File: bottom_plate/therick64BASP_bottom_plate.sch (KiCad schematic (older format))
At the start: 80 parts, among them U1 HOLE, U10 HOLE, U11 HOLE, U12 HOLE, U13 HOLE, U14 HOLE, U15 HOLE, U16 HOLE, U17 HOLE, U18 HOLE, U19 HOLE, U2 HOLE, U20 HOLE, U21 HOLE, U22 HOLE, U23 HOLE, U24 HOLE, U25 HOLE, U26 HOLE, U27 HOLE, U28 HOLE, U29 HOLE, U3 HOLE, U30 HOLE, U31 HOLE, U32 HOLE, U33 HOLE, U34 HOLE, U35 HOLE, U36 HOLE, U37 HOLE, U38 HOLE, U39 HOLE, U4 HOLE, U40 HOLE, U41 HOLE, U42 HOLE, U43 HOLE, U44 HOLE, U45 HOLE, U46 HOLE, U47 HOLE, U48 HOLE, U49 HOLE, U5 HOLE, U50 HOLE, U51 HOLE, U52 HOLE, U53 HOLE, U54 HOLE, U55 HOLE, U56 HOLE, U57 HOLE, U58 HOLE, U59 HOLE, U6 HOLE, U60 HOLE, U61 HOLE, U62 HOLE, U63 HOLE, U64 HOLE, U65 HOLE, U66 HOLE, U67 HOLE, U68 HOLE, U69 HOLE, U7 HOLE, U70 HOLE, U8 HOLE, U9 HOLE

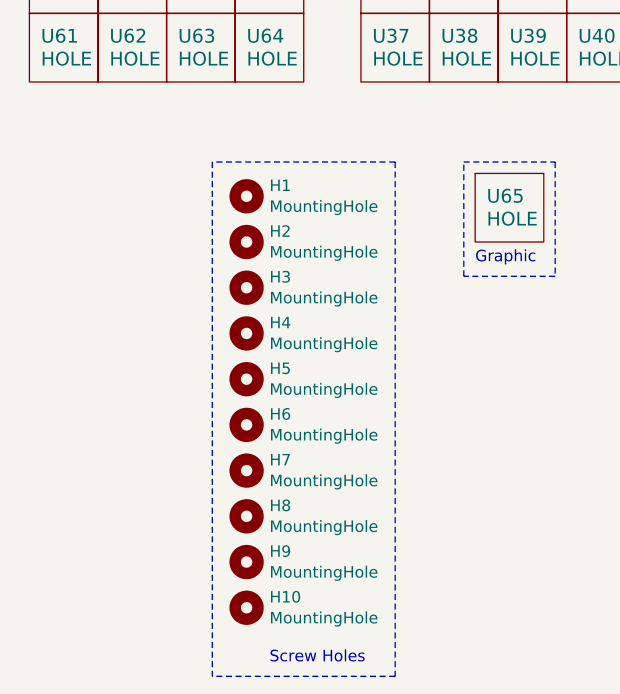
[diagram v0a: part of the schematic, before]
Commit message: Remapped ISP Flash, added mounting holes
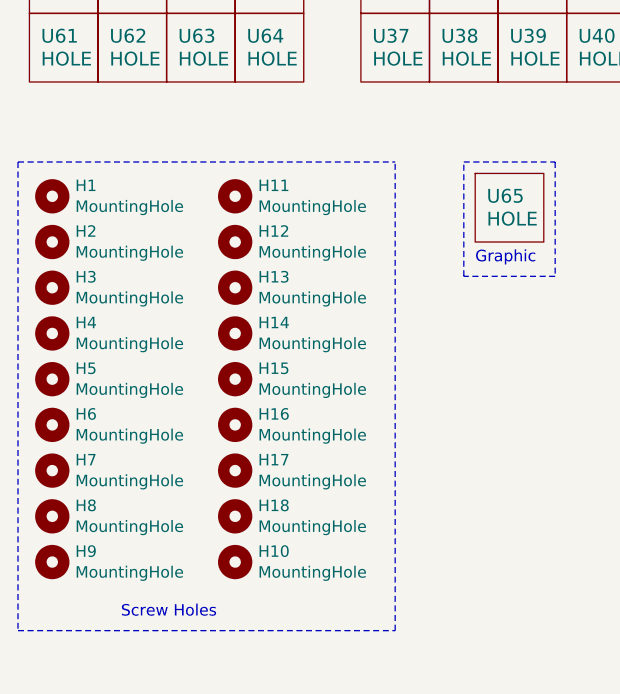
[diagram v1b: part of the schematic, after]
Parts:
- added H11, H12, H13, H14, H15, H16, H17, H18: MountingHole, random-keyboard-parts:Generic-Mounthole, symbol Mechanical:MountingHole
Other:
- moved on the sheet: H1, H10, H2, H3, H4, H5, H6, H7, H8, H9
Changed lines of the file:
@@
 L Mechanical:MountingHole H2
 U 1 1 5DAFB0AC
-P 2000 3300
-F 0 "H2" H 2100 3346 50  0000 L CNN
-F 1 "MountingHole" H 2100 3255 50  0000 L CNN
-F 2 "random-keyboard-parts:Generic-Mounthole" H 2000 3300 50  0001 C CNN
-F 3 "~" H 2000 3300 50  0001 C CNN
-	1    2000 3300
+P 1150 3300
+F 0 "H2" H 1250 3346 50  0000 L CNN
+F 1 "MountingHole" H 1250 3255 50  0000 L CNN
+F 2 "random-keyboard-parts:Generic-Mounthole" H 1150 3300 50  0001 C CNN
+F 3 "~" H 1150 3300 50  0001 C CNN
+	1    1150 3300
 	1    0    0    -1
 $EndComp
@@
 L Mechanical:MountingHole H1
 U 1 1 5DAFBA19
-P 2000 3100
-F 0 "H1" H 2100 3146 50  0000 L CNN
-F 1 "MountingHole" H 2100 3055 50  0000 L CNN
-F 2 "random-keyboard-parts:Generic-Mounthole" H 2000 3100 50  0001 C CNN
-F 3 "~" H 2000 3100 50  0001 C CNN
-	1    2000 3100
+P 1150 3100
+F 0 "H1" H 1250 3146 50  0000 L CNN
+F 1 "MountingHole" H 1250 3055 50  0000 L CNN
+F 2 "random-keyboard-parts:Generic-Mounthole" H 1150 3100 50  0001 C CNN
+F 3 "~" H 1150 3100 50  0001 C CNN
+	1    1150 3100
 	1    0    0    -1
 $EndComp
@@
 L Mechanical:MountingHole H3
 U 1 1 5DAFC41A
-P 2000 3500
-F 0 "H3" H 2100 3546 50  0000 L CNN
-F 1 "MountingHole" H 2100 3455 50  0000 L CNN
-F 2 "random-keyboard-parts:Generic-Mounthole" H 2000 3500 50  0001 C CNN
-F 3 "~" H 2000 3500 50  0001 C CNN
-	1    2000 3500
+P 1150 3500
+F 0 "H3" H 1250 3546 50  0000 L CNN
+F 1 "MountingHole" H 1250 3455 50  0000 L CNN
+F 2 "random-keyboard-parts:Generic-Mounthole" H 1150 3500 50  0001 C CNN
+F 3 "~" H 1150 3500 50  0001 C CNN
+	1    1150 3500
 	1    0    0    -1
 $EndComp
@@
 L Mechanical:MountingHole H4
 U 1 1 5DAFCFC0
-P 2000 3700
-F 0 "H4" H 2100 3746 50  0000 L CNN
-F 1 "MountingHole" H 2100 3655 50  0000 L CNN
-F 2 "random-keyboard-parts:Generic-Mounthole" H 2000 3700 50  0001 C CNN
-F 3 "~" H 2000 3700 50  0001 C CNN
-	1    2000 3700
+P 1150 3700
+F 0 "H4" H 1250 3746 50  0000 L CNN
+F 1 "MountingHole" H 1250 3655 50  0000 L CNN
+F 2 "random-keyboard-parts:Generic-Mounthole" H 1150 3700 50  0001 C CNN
+F 3 "~" H 1150 3700 50  0001 C CNN
+	1    1150 3700
 	1    0    0    -1
 $EndComp
@@
 L Mechanical:MountingHole H5
 U 1 1 5DAFD908
-P 2000 3900
-F 0 "H5" H 2100 3946 50  0000 L CNN
-F 1 "MountingHole" H 2100 3855 50  0000 L CNN
-F 2 "random-keyboard-parts:Generic-Mounthole" H 2000 3900 50  0001 C CNN
-F 3 "~" H 2000 3900 50  0001 C CNN
-	1    2000 3900
+P 1150 3900
+F 0 "H5" H 1250 3946 50  0000 L CNN
+F 1 "MountingHole" H 1250 3855 50  0000 L CNN
+F 2 "random-keyboard-parts:Generic-Mounthole" H 1150 3900 50  0001 C CNN
+F 3 "~" H 1150 3900 50  0001 C CNN
+	1    1150 3900
 	1    0    0    -1
 $EndComp
@@
 L Mechanical:MountingHole H6
 U 1 1 5DAFE1B7
-P 2000 4100
-F 0 "H6" H 2100 4146 50  0000 L CNN
-F 1 "MountingHole" H 2100 4055 50  0000 L CNN
-F 2 "random-keyboard-parts:Generic-Mounthole" H 2000 4100 50  0001 C CNN
-F 3 "~" H 2000 4100 50  0001 C CNN
-	1    2000 4100
+P 1150 4100
+F 0 "H6" H 1250 4146 50  0000 L CNN
+F 1 "MountingHole" H 1250 4055 50  0000 L CNN
+F 2 "random-keyboard-parts:Generic-Mounthole" H 1150 4100 50  0001 C CNN
+F 3 "~" H 1150 4100 50  0001 C CNN
+	1    1150 4100
 	1    0    0    -1
 $EndComp
@@
 	1    0    0    -1
 $EndComp
-Text Notes 2100 5150 0    50   ~ 0
+Text Notes 1450 4950 0    50   ~ 0
 Screw Holes
-Wire Notes Line
-	2650 2950 1850 2950
 Text Notes 3000 3400 0    50   ~ 0
 Graphic
@@
 L Mechanical:MountingHole H8
 U 1 1 5F465E60
-P 2000 4500
-F 0 "H8" H 2100 4546 50  0000 L CNN
-F 1 "MountingHole" H 2100 4455 50  0000 L CNN
-F 2 "random-keyboard-parts:Generic-Mounthole" H 2000 4500 50  0001 C CNN
-F 3 "~" H 2000 4500 50  0001 C CNN
-	1    2000 4500
+P 1150 4500
+F 0 "H8" H 1250 4546 50  0000 L CNN
+F 1 "MountingHole" H 1250 4455 50  0000 L CNN
+F 2 "random-keyboard-parts:Generic-Mounthole" H 1150 4500 50  0001 C CNN
+F 3 "~" H 1150 4500 50  0001 C CNN
+	1    1150 4500
 	1    0    0    -1
 $EndComp
@@
 L Mechanical:MountingHole H7
 U 1 1 5F465E66
-P 2000 4300
-F 0 "H7" H 2100 4346 50  0000 L CNN
-F 1 "MountingHole" H 2100 4255 50  0000 L CNN
-F 2 "random-keyboard-parts:Generic-Mounthole" H 2000 4300 50  0001 C CNN
-F 3 "~" H 2000 4300 50  0001 C CNN
-	1    2000 4300
+P 1150 4300
+F 0 "H7" H 1250 4346 50  0000 L CNN
+F 1 "MountingHole" H 1250 4255 50  0000 L CNN
+F 2 "random-keyboard-parts:Generic-Mounthole" H 1150 4300 50  0001 C CNN
+F 3 "~" H 1150 4300 50  0001 C CNN
+	1    1150 4300
 	1    0    0    -1
 $EndComp
@@
 L Mechanical:MountingHole H9
 U 1 1 5F465E6C
-P 2000 4700
-F 0 "H9" H 2100 4746 50  0000 L CNN
-F 1 "MountingHole" H 2100 4655 50  0000 L CNN
-F 2 "random-keyboard-parts:Generic-Mounthole" H 2000 4700 50  0001 C CNN
-F 3 "~" H 2000 4700 50  0001 C CNN
-	1    2000 4700
+P 1150 4700
+F 0 "H9" H 1250 4746 50  0000 L CNN
+F 1 "MountingHole" H 1250 4655 50  0000 L CNN
+F 2 "random-keyboard-parts:Generic-Mounthole" H 1150 4700 50  0001 C CNN
+F 3 "~" H 1150 4700 50  0001 C CNN
+	1    1150 4700
 	1    0    0    -1
 $EndComp
@@
 L Mechanical:MountingHole H10
 U 1 1 5F465E72
-P 2000 4900
-F 0 "H10" H 2100 4946 50  0000 L CNN
-F 1 "MountingHole" H 2100 4855 50  0000 L CNN
-F 2 "random-keyboard-parts:Generic-Mounthole" H 2000 4900 50  0001 C CNN
-F 3 "~" H 2000 4900 50  0001 C CNN
-	1    2000 4900
-	1    0    0    -1
-$EndComp
-Wire Notes Line
-	2650 5200 1850 5200
-Wire Notes Line
-	1850 2950 1850 5200
-Wire Notes Line
-	2650 2950 2650 5200
+P 1950 4700
+F 0 "H10" H 2050 4746 50  0000 L CNN
+F 1 "MountingHole" H 2050 4655 50  0000 L CNN
+F 2 "random-keyboard-parts:Generic-Mounthole" H 1950 4700 50  0001 C CNN
+F 3 "~" H 1950 4700 50  0001 C CNN
+	1    1950 4700
+	1    0    0    -1
+$EndComp
 Text Notes 4100 3900 0    50   ~ 0
 Mouse\nBites
@@
 Wire Notes Line
 	3350 3450 2950 3450
+$Comp
+L Mechanical:MountingHole H12
+U 1 1 5EBEEE9D
+P 1950 3300
+F 0 "H12" H 2050 3346 50  0000 L CNN
+F 1 "MountingHole" H 2050 3255 50  0000 L CNN
+F 2 "random-keyboard-parts:Generic-Mounthole" H 1950 3300 50  0001 C CNN
+F 3 "~" H 1950 3300 50  0001 C CNN
+	1    1950 3300
+	1    0    0    -1
+$EndComp
+$Comp
+L Mechanical:MountingHole H11
+U 1 1 5EBEEEA3
+P 1950 3100
+F 0 "H11" H 2050 3146 50  0000 L CNN
+F 1 "MountingHole" H 2050 3055 50  0000 L CNN
+F 2 "random-keyboard-parts:Generic-Mounthole" H 1950 3100 50  0001 C CNN
+F 3 "~" H 1950 3100 50  0001 C CNN
+	1    1950 3100
+	1    0    0    -1
+$EndComp
+$Comp
+L Mechanical:MountingHole H13
+U 1 1 5EBEEEA9
+P 1950 3500
+F 0 "H13" H 2050 3546 50  0000 L CNN
+F 1 "MountingHole" H 2050 3455 50  0000 L CNN
+F 2 "random-keyboard-parts:Generic-Mounthole" H 1950 3500 50  0001 C CNN
+F 3 "~" H 1950 3500 50  0001 C CNN
+	1    1950 3500
+	1    0    0    -1
+$EndComp
+$Comp
+L Mechanical:MountingHole H14
+U 1 1 5EBEEEAF
+P 1950 3700
+F 0 "H14" H 2050 3746 50  0000 L CNN
+F 1 "MountingHole" H 2050 3655 50  0000 L CNN
+F 2 "random-keyboard-parts:Generic-Mounthole" H 1950 3700 50  0001 C CNN
+F 3 "~" H 1950 3700 50  0001 C CNN
+	1    1950 3700
+	1    0    0    -1
+$EndComp
+$Comp
+L Mechanical:MountingHole H15
+U 1 1 5EBEEEB5
+P 1950 3900
+F 0 "H15" H 2050 3946 50  0000 L CNN
+F 1 "MountingHole" H 2050 3855 50  0000 L CNN
+F 2 "random-keyboard-parts:Generic-Mounthole" H 1950 3900 50  0001 C CNN
+F 3 "~" H 1950 3900 50  0001 C CNN
+	1    1950 3900
+	1    0    0    -1
+$EndComp
+$Comp
+L Mechanical:MountingHole H16
+U 1 1 5EBEEEBB
+P 1950 4100
+F 0 "H16" H 2050 4146 50  0000 L CNN
+F 1 "MountingHole" H 2050 4055 50  0000 L CNN
+F 2 "random-keyboard-parts:Generic-Mounthole" H 1950 4100 50  0001 C CNN
+F 3 "~" H 1950 4100 50  0001 C CNN
+	1    1950 4100
+	1    0    0    -1
+$EndComp
+$Comp
+L Mechanical:MountingHole H18
+U 1 1 5EBEEEC1
+P 1950 4500
+F 0 "H18" H 2050 4546 50  0000 L CNN
+F 1 "MountingHole" H 2050 4455 50  0000 L CNN
+F 2 "random-keyboard-parts:Generic-Mounthole" H 1950 4500 50  0001 C CNN
+F 3 "~" H 1950 4500 50  0001 C CNN
+	1    1950 4500
+	1    0    0    -1
+$EndComp
+$Comp
+L Mechanical:MountingHole H17
+U 1 1 5EBEEEC7
+P 1950 4300
+F 0 "H17" H 2050 4346 50  0000 L CNN
+F 1 "MountingHole" H 2050 4255 50  0000 L CNN
+F 2 "random-keyboard-parts:Generic-Mounthole" H 1950 4300 50  0001 C CNN
+F 3 "~" H 1950 4300 50  0001 C CNN
+	1    1950 4300
+	1    0    0    -1
+$EndComp
+Wire Notes Line
+	1000 2950 1000 5000
+Wire Notes Line
+	1000 5000 2650 5000
+Wire Notes Line
+	2650 5000 2650 2950
+Wire Notes Line
+	1000 2950 2650 2950
 $EndSCHEMATC

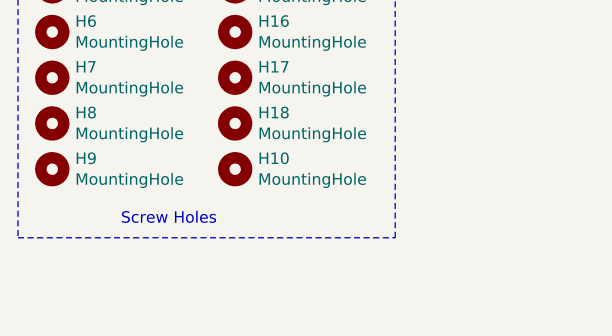
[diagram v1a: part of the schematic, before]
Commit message: Add reset hole
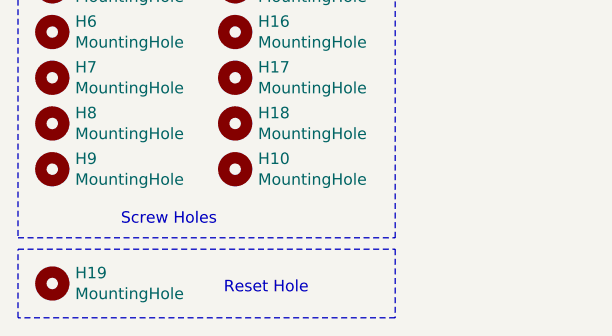
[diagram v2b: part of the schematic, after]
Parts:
- added H19: MountingHole, random-keyboard-parts:Generic-Mounthole, symbol Mechanical:MountingHole
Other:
- note added: "Reset Hole"
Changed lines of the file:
@@
 Wire Notes Line
 	1000 2950 2650 2950
+$Comp
+L Mechanical:MountingHole H19
+U 1 1 5EBF4BCA
+P 1150 5200
+F 0 "H19" H 1250 5246 50  0000 L CNN
+F 1 "MountingHole" H 1250 5155 50  0000 L CNN
+F 2 "random-keyboard-parts:Generic-Mounthole" H 1150 5200 50  0001 C CNN
+F 3 "~" H 1150 5200 50  0001 C CNN
+	1    1150 5200
+	1    0    0    -1
+$EndComp
+Text Notes 1900 5250 0    50   ~ 0
+Reset Hole
+Wire Notes Line
+	1000 5050 2650 5050
+Wire Notes Line
+	2650 5050 2650 5350
+Wire Notes Line
+	2650 5350 1000 5350
+Wire Notes Line
+	1000 5350 1000 5050
 $EndSCHEMATC
